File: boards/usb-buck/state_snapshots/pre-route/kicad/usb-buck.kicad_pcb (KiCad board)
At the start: 4 copper layers, 50 x 40 mm, 28 parts, among them J1 USB Micro-B receptacle SMD, J2 1x4 2.54mm male THT, SW1 SMD tactile switch, U1 STM32F103C8T6, U2 AP63203QWU-7, U3 USBLC6-2SC6, Y1 8MHz 20pF

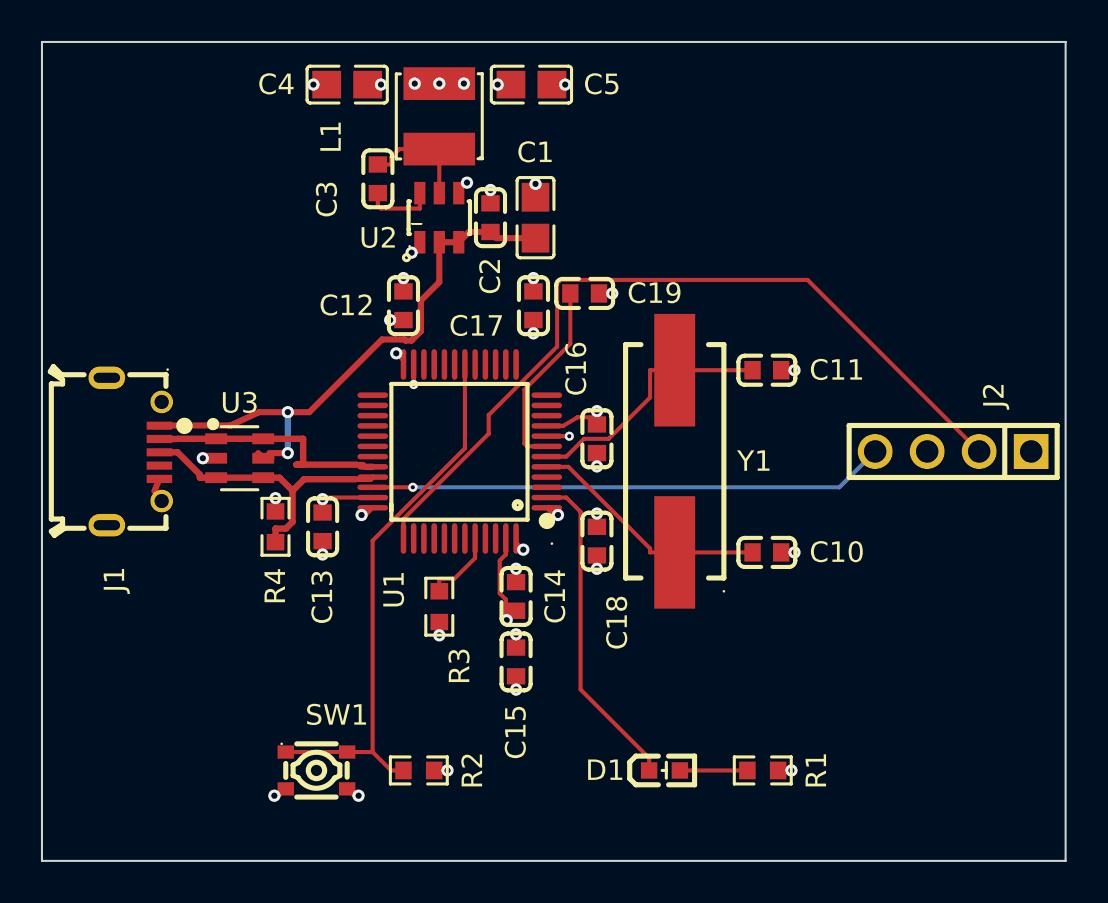
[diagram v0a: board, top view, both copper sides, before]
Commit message: ai-ee usb-buck: drc_routed pass (4L chain; 4 router-found defects fixed in-run)
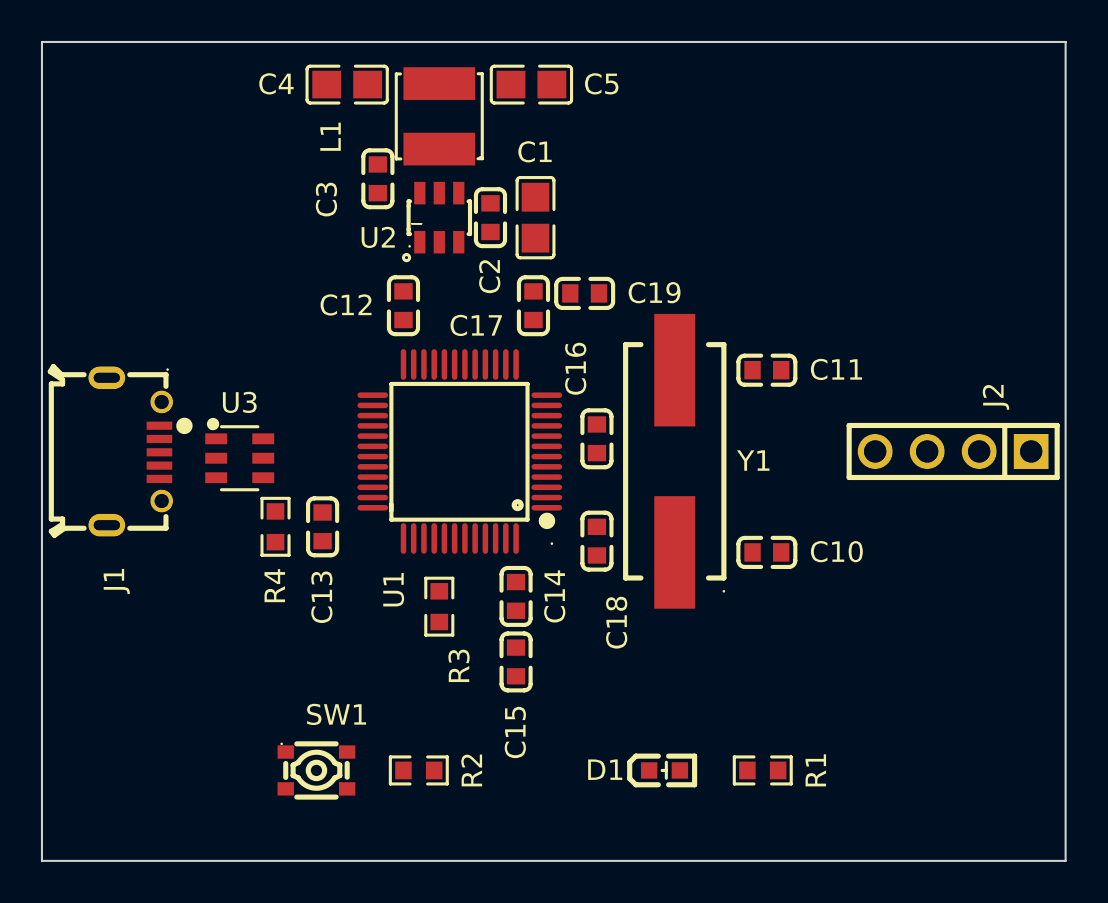
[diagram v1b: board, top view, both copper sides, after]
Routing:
- net /mcu/SWCLK: track 39.7 -> 0.00 mm
- net GND: track 29.8 -> 0.00 mm, vias 21 -> 0
- net VBUS: track 28.0 -> 0.00 mm, vias 2 -> 0
- net /mcu/BTN: track 26.9 -> 0.00 mm
- net /mcu/SWDIO: track 25.3 -> 0.00 mm, vias 1 -> 0
- net +3V3: track 16.8 -> 0.00 mm, vias 20 -> 0
- net /mcu/LED: track 16.0 -> 0.00 mm
- net /USB_DP: track 14.7 -> 0.00 mm
- net /mcu/OSC_OUT: track 12.6 -> 0.00 mm
- net /USB_DM: track 12.4 -> 0.00 mm
- net /mcu/OSC_IN: track 11.9 -> 0.00 mm
- net /mcu/NRST: track 9.41 -> 0.00 mm
- net /power/SW: track 5.67 -> 0.00 mm
- net /mcu/BOOT0: track 3.73 -> 0.00 mm
- net /power/BST: track 3.47 -> 0.00 mm
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- removed copper zone on In2.Cu, net +3V3
- removed copper zone on In1.Cu, net GND
